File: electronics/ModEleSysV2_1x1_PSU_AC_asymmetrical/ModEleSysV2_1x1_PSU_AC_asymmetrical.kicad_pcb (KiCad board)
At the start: 2 copper layers, 43.2 x 49.5 mm, 38 parts, among them J2 Jack-DC, SW1 switch_DPDT, U1 LM317, U2 LM337

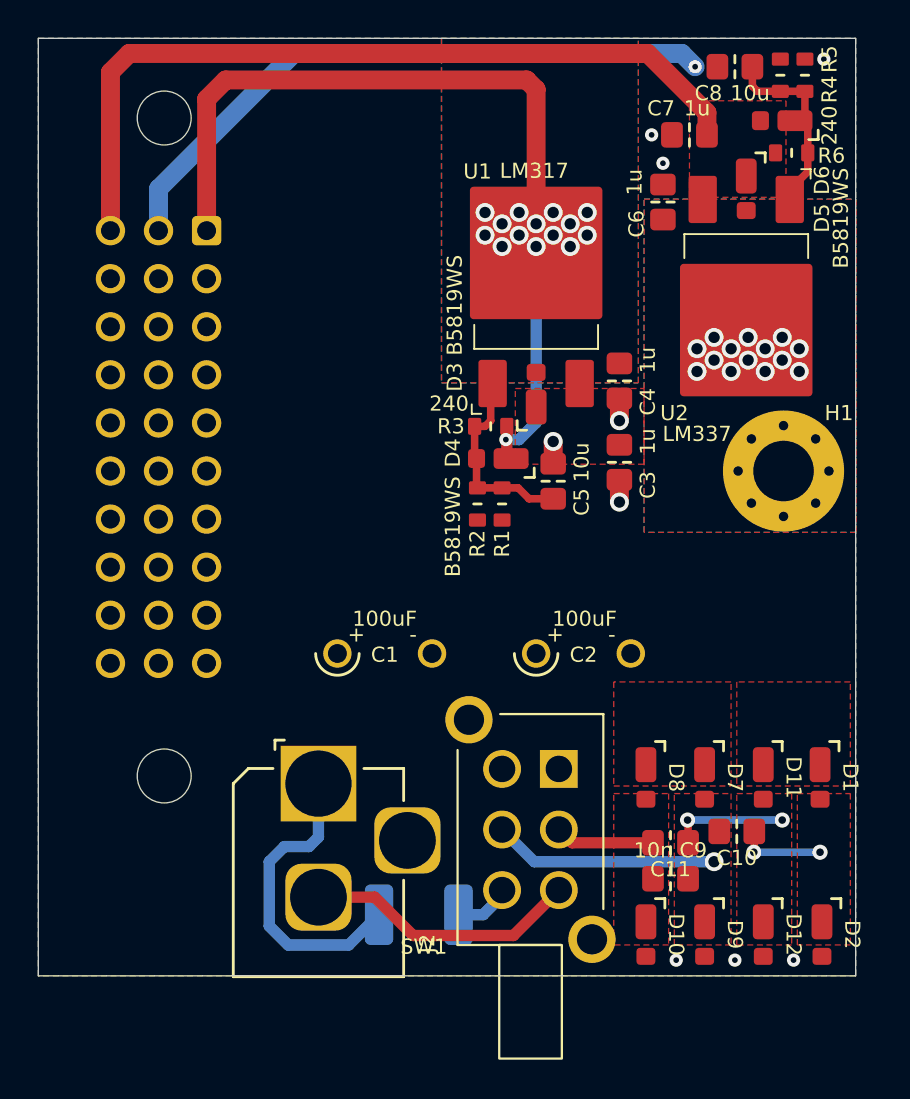
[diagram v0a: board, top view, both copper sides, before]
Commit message: added second regulator
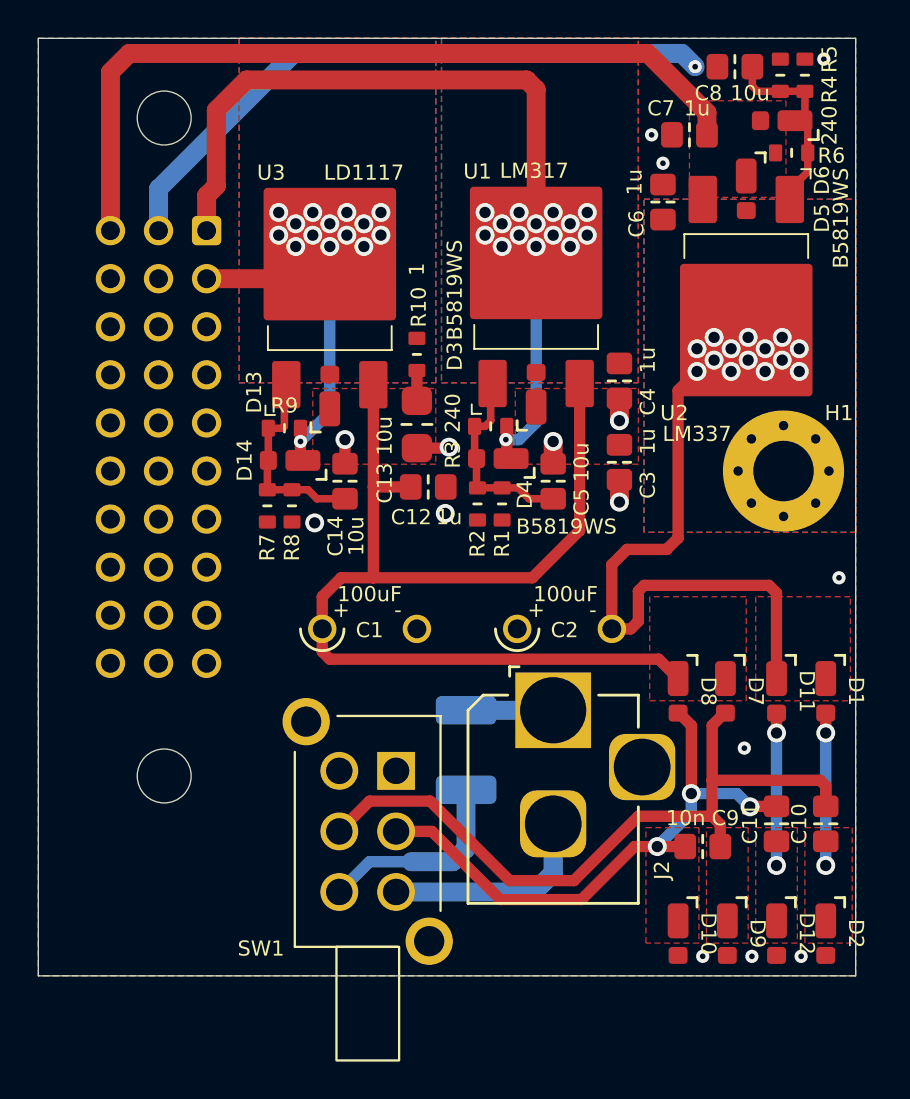
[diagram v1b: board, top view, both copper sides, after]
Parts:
- added C12: 1u, SquantorCapacitor:C_0805+0603, F.Cu at (160.3, 87.2)
- added C13: 10u, SquantorCapacitor:C_1206_0805, F.Cu at (159.7, 83.9)
- added C14: 10u, SquantorCapacitor:C_0805+0603, F.Cu at (155.9, 86.9)
- added D13: B5819WS, SquantorDiodes:SOD-323HE-shikues, F.Cu at (155.1, 82.4)
- added D14: B5819WS, SquantorDiodes:SOD-323HE-shikues, F.Cu at (153.0, 85.8)
- added R10: 1, SquantorResistor:R_0603_hand, F.Cu at (159.7, 80.2)
- added R7: TBD, SquantorResistor:R_0603_hand, F.Cu at (151.8, 88.2)
- added R8: TBD, SquantorResistor:R_0603_hand, F.Cu at (153.1, 88.2)
- added R9: 120, SquantorResistor:R_0603_hand, F.Cu at (152.7, 84.1)
- added U3: LD1117, SquantorIC:TO-252_D-PAK_IRF, F.Cu at (155.1, 74.9)
- moved J2 13.0 mm to (166.9, 99.0)
- moved F1 9.05 mm to (162.3, 101.1), turned to 90 degrees
- moved SW1 8.60 mm to (157.1, 105.4)
- moved C11 5.69 mm to (178.7, 105.0), turned to 90 degrees
- moved D8 4.86 mm to (173.5, 98.0)
- moved C10 4.72 mm to (181.3, 105.0), turned to 90 degrees
- moved D7 4.68 mm to (176.0, 98.0)
- moved D11 4.60 mm to (178.7, 98.0)
- moved D1 4.56 mm to (181.3, 98.0)
- moved C9 2.40 mm to (174.8, 106.2)
- moved D10 1.70 mm to (173.5, 110.8)
- moved C2 1.64 mm to (167.5, 94.7)
- moved C1 1.53 mm to (157.2, 94.7)
- moved D9 1.20 mm to (176.1, 110.8)
- moved D12 0.70 mm to (178.7, 110.8)
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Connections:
- net /+adj renamed /+adj1
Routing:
- net /DC1p: track 0.00 -> 57.3 mm
- net /DC1n: track 0.00 -> 32.0 mm
- net /AC1_PHASE: track 11.9 -> 38.3 mm, vias 1 -> 0
- net /AC_NEUT: track 5.26 -> 30.8 mm, vias 0 -> 3
- net /+5V: track 0.00 -> 19.7 mm, vias 0 -> 15
- net Net-(F1-Pad2): track 16.2 -> 4.60 mm
- net /+adj2: track 0.00 -> 10.7 mm
- net /AC_PHASE1_IN: track 3.01 -> 10.8 mm
- net /AC_PHASE_NEG: track 4.61 -> 8.05 mm
- net /AC_NEUT_IN: track 14.5 -> 11.3 mm
- net GND: track 37.3 -> 40.3 mm, vias 10 -> 16
- net /AC_NEUT_NEG: track 6.21 -> 8.05 mm
- net Net-(C13-Pad1): track 0.00 -> 1.60 mm
- net /+aV: track 45.2 -> 44.5 mm
- added copper zone on B.Cu, net /+5V
- added copper zone on F.Cu, net /+5V

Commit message: silk placement done
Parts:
- R10: value 1 -> 1R
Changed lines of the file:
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@@
         (effects (font (size 0.8 0.8) (thickness 0.15)))
     )
-    (fp_text value "B5819WS" (at 2.4 -3.9 90 unlocked) (layer "F.Fab")
+    (fp_text value "B5819WS" (at 2.4 -4.1 90 unlocked) (layer "F.SilkS")
         (effects (font (size 0.8 0.8) (thickness 0.15)))
     )
@@
     (property "ki_keywords" "R res resistor")
     (attr smd)
-    (fp_text reference "R3" (at -2 1.5 90) (layer "F.SilkS")
-        (effects (font (size 0.8 0.8) (thickness 0.15)))
-    )
-    (fp_text value "240" (at -2 -0.7 90) (layer "F.SilkS")
+    (fp_text reference "R3" (at -2.1 0 180) (layer "F.SilkS")
+        (effects (font (size 0.8 0.8) (thickness 0.15)))
+    )
+    (fp_text value "240" (at -1.6 -1.9 -90) (layer "F.SilkS")
         (effects (font (size 0.8 0.8) (thickness 0.15)))
     )
@@
     (property "ki_keywords" "R res resistor")
     (attr smd)
-    (fp_text reference "R9" (at 0 -1.2) (layer "F.SilkS")
-        (effects (font (size 0.8 0.8) (thickness 0.15)))
-    )
-    (fp_text value "120" (at 0 1.2) (layer "F.Fab")
+    (fp_text reference "R9" (at -2.2 0) (layer "F.SilkS")
+        (effects (font (size 0.8 0.8) (thickness 0.15)))
+    )
+    (fp_text value "120" (at -2.1 -1.3) (layer "F.SilkS")
         (effects (font (size 0.8 0.8) (thickness 0.15)))
     )
@@
     (property "ki_keywords" "diode")
     (attr smd)
-    (fp_text reference "D3" (at 2 -4.3 90 unlocked) (layer "F.SilkS")
-        (effects (font (size 0.8 0.8) (thickness 0.15)))
-    )
-    (fp_text value "B5819WS" (at 5.5 -4.3 90 unlocked) (layer "F.SilkS")
+    (fp_text reference "D3" (at 2.2 -4.4 90 unlocked) (layer "F.SilkS")
+        (effects (font (size 0.8 0.8) (thickness 0.15)))
+    )
+    (fp_text value "B5819WS" (at 6 -4.4 90 unlocked) (layer "F.SilkS")
         (effects (font (size 0.8 0.8) (thickness 0.15)))
     )
@@
     (property "ki_keywords" "diode")
     (attr smd)
-    (fp_text reference "D13" (at 0.2 -4 90 unlocked) (layer "F.SilkS")
-        (effects (font (size 0.8 0.8) (thickness 0.15)))
-    )
-    (fp_text value "B5819WS" (at 4.1 -4 90 unlocked) (layer "F.Fab")
+    (fp_text reference "D13" (at 2.2 -4.3 90 unlocked) (layer "F.SilkS")
+        (effects (font (size 0.8 0.8) (thickness 0.15)))
+    )
+    (fp_text value "B5819WS" (at 6.3 -4.3 90 unlocked) (layer "F.SilkS")
         (effects (font (size 0.8 0.8) (thickness 0.15)))
     )
@@
     (property "ki_keywords" "R res resistor")
     (attr smd)
-    (fp_text reference "R10" (at -2.5 -0.1 90) (layer "F.SilkS")
-        (effects (font (size 0.8 0.8) (thickness 0.15)))
-    )
-    (fp_text value "1" (at -4.5 0 90) (layer "F.SilkS")
-        (effects (font (size 0.8 0.8) (thickness 0.15)))
-    )
+    (fp_text reference "R10" (at -2.5 0 90) (layer "F.SilkS")
+        (effects (font (size 0.8 0.8) (thickness 0.15)))
+    )
+    (fp_text value "1R" (at -4.8 0 90) (layer "F.SilkS")
+        (effects (font (size 0.8 0.8) (thickness 0.15)))
+    )

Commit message: reviewed
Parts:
- C4, C7: footprint SquantorCapacitor:C_0805+0603 -> SquantorCapacitor:C_1206_0805
- N1: value 20240329 -> 20240424
- moved C7 0.81 mm to (173.7, 67.9)
- moved C4 0.63 mm to (170.6, 81.0)
- moved C2 0.30 mm to (167.8, 94.7)
- moved C6 0.25 mm to (172.7, 71.9)
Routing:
- net /-aV: track 42.8 -> 41.9 mm
- net /+aV: track 44.5 -> 45.2 mm

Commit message: updated versionnumbers
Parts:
- N1: value 20240424 -> 20240426
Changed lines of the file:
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@@
     (property "ki_keywords" "diode")
     (attr smd)
-    (fp_text reference "D10" (at 0 -1.6 -90 unlocked) (layer "F.SilkS")
+    (fp_text reference "D10" (at -2.5 0 unlocked) (layer "F.SilkS")
         (effects (font (size 0.8 0.8) (thickness 0.15)))
     )
@@
     (property "ki_keywords" "cap capacitor")
     (attr smd)
-    (fp_text reference "C11" (at 0 -1.4 90) (layer "F.SilkS")
-        (effects (font (size 0.8 0.8) (thickness 0.15)))
-    )
-    (fp_text value "10u" (at 0 1.5 90) (layer "F.Fab")
+    (fp_text reference "C11" (at 2.3 0 180) (layer "F.SilkS")
+        (effects (font (size 0.8 0.8) (thickness 0.15)))
+    )
+    (fp_text value "10u" (at 3.4 0 180) (layer "F.SilkS")
         (effects (font (size 0.8 0.8) (thickness 0.15)))
     )
@@
         (effects (font (size 0.8 0.8) (thickness 0.15)))
     )
-    (fp_text value "120" (at -2.1 -1.3) (layer "F.SilkS")
+    (fp_text value "120" (at -2.2 -1.3) (layer "F.SilkS")
         (effects (font (size 0.8 0.8) (thickness 0.15)))
     )
@@
     (property "ki_keywords" "DC power barrel jack connector")
     (attr through_hole)
-    (fp_text reference "J2" (at -8.45 5.75 90) (layer "F.SilkS")
+    (fp_text reference "J2" (at 1.5 3) (layer "F.SilkS")
         (effects (font (size 0.8 0.8) (thickness 0.15)))
     )
@@
     (property "ki_keywords" "diode")
     (attr smd)
-    (fp_text reference "D8" (at 0 -1.6 -90 unlocked) (layer "F.SilkS")
-        (effects (font (size 0.8 0.8) (thickness 0.15)))
-    )
-    (fp_text value "B5819WSE" (at 0 1.5 -90 unlocked) (layer "F.Fab")
+    (fp_text reference "D8" (at -2.5 -0.1 unlocked) (layer "F.SilkS")
+        (effects (font (size 0.8 0.8) (thickness 0.15)))
+    )
+    (fp_text value "B5819WSE" (at 2.5 -3.5 unlocked) (layer "F.SilkS")
         (effects (font (size 0.8 0.8) (thickness 0.15)))
     )
@@
     (property "ki_keywords" "diode")
     (attr smd)
-    (fp_text reference "D11" (at 0 -1.6 -90 unlocked) (layer "F.SilkS")
+    (fp_text reference "D11" (at -2.5 0 unlocked) (layer "F.SilkS")
         (effects (font (size 0.8 0.8) (thickness 0.15)))
     )
@@
     (property "ki_keywords" "diode")
     (attr smd)
-    (fp_text reference "D2" (at 0 -1.6 -90 unlocked) (layer "F.SilkS")
+    (fp_text reference "D2" (at -2.5 0.4 unlocked) (layer "F.SilkS")
         (effects (font (size 0.8 0.8) (thickness 0.15)))
     )
@@
     (property "ki_keywords" "diode")
     (attr smd)
-    (fp_text reference "D1" (at 0 -1.6 -90 unlocked) (layer "F.SilkS")
+    (fp_text reference "D1" (at -2.5 0 unlocked) (layer "F.SilkS")
         (effects (font (size 0.8 0.8) (thickness 0.15)))
     )
@@
     (property "ki_keywords" "diode")
     (attr smd)
-    (fp_text reference "D12" (at 0 -1.6 -90 unlocked) (layer "F.SilkS")
+    (fp_text reference "D12" (at -2.5 0 unlocked) (layer "F.SilkS")
         (effects (font (size 0.8 0.8) (thickness 0.15)))
     )
@@
     (property "ki_keywords" "diode")
     (attr smd)
-    (fp_text reference "D9" (at 0 -1.6 -90 unlocked) (layer "F.SilkS")
+    (fp_text reference "D9" (at -2.5 0.3 unlocked) (layer "F.SilkS")
         (effects (font (size 0.8 0.8) (thickness 0.15)))
     )
@@
     (property "ki_keywords" "cap capacitor")
     (attr smd)
-    (fp_text reference "C10" (at 0 -1.4 90) (layer "F.SilkS")
-        (effects (font (size 0.8 0.8) (thickness 0.15)))
-    )
-    (fp_text value "10u" (at 0 1.5 90) (layer "F.Fab")
+    (fp_text reference "C10" (at 2.3 0 180) (layer "F.SilkS")
+        (effects (font (size 0.8 0.8) (thickness 0.15)))
+    )
+    (fp_text value "10u" (at 3.4 0 180) (layer "F.SilkS")
         (effects (font (size 0.8 0.8) (thickness 0.15)))
     )
@@
     (property "ki_keywords" "diode")
     (attr smd)
-    (fp_text reference "D7" (at 0 -1.6 -90 unlocked) (layer "F.SilkS")
+    (fp_text reference "D7" (at -2.5 0 unlocked) (layer "F.SilkS")
         (effects (font (size 0.8 0.8) (thickness 0.15)))
     )
@@
         (effects (font (size 1 1) (thickness 0.15)) (justify mirror))
     )
-    (fp_text value "20240424" (at 0.8 0.1) (layer "B.SilkS")
+    (fp_text value "20240426" (at 0.8 0.1) (layer "B.SilkS")
         (effects (font (size 0.8 0.8) (thickness 0.15)) (justify mirror))
     )
@@
     (property "ki_keywords" "fuse")
     (attr smd)
-    (fp_text reference "F1" (at 2.575 -2.555 90 unlocked) (layer "B.SilkS")
+    (fp_text reference "F1" (at -3.9 -1.5 90 unlocked) (layer "B.SilkS")
         (effects (font (size 0.8 0.8) (thickness 0.15)) (justify mirror))
     )
-    (fp_text value "0.6A 60V" (at -1.025 -2.555 90 unlocked) (layer "B.SilkS")
+    (fp_text value "0.6A 60V" (at -5.9 -0.4 90 unlocked) (layer "B.SilkS")
         (effects (font (size 0.8 0.8) (thickness 0.15)) (justify mirror))
     )
